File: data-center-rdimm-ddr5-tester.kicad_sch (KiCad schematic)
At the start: 2 parts

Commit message: [#80386] Add company name in board settings
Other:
- company: (none) -> Antmicro
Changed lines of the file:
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@@
 		(date "2023-07-27")
 		(rev "1.0.1")
+		(company "Antmicro")
 		(comment 1 "www.antmicro.com")
-		(comment 2 "Antmicro Ltd")
 	)
 	(text "Data Center RDIMM DDR5 Tester"

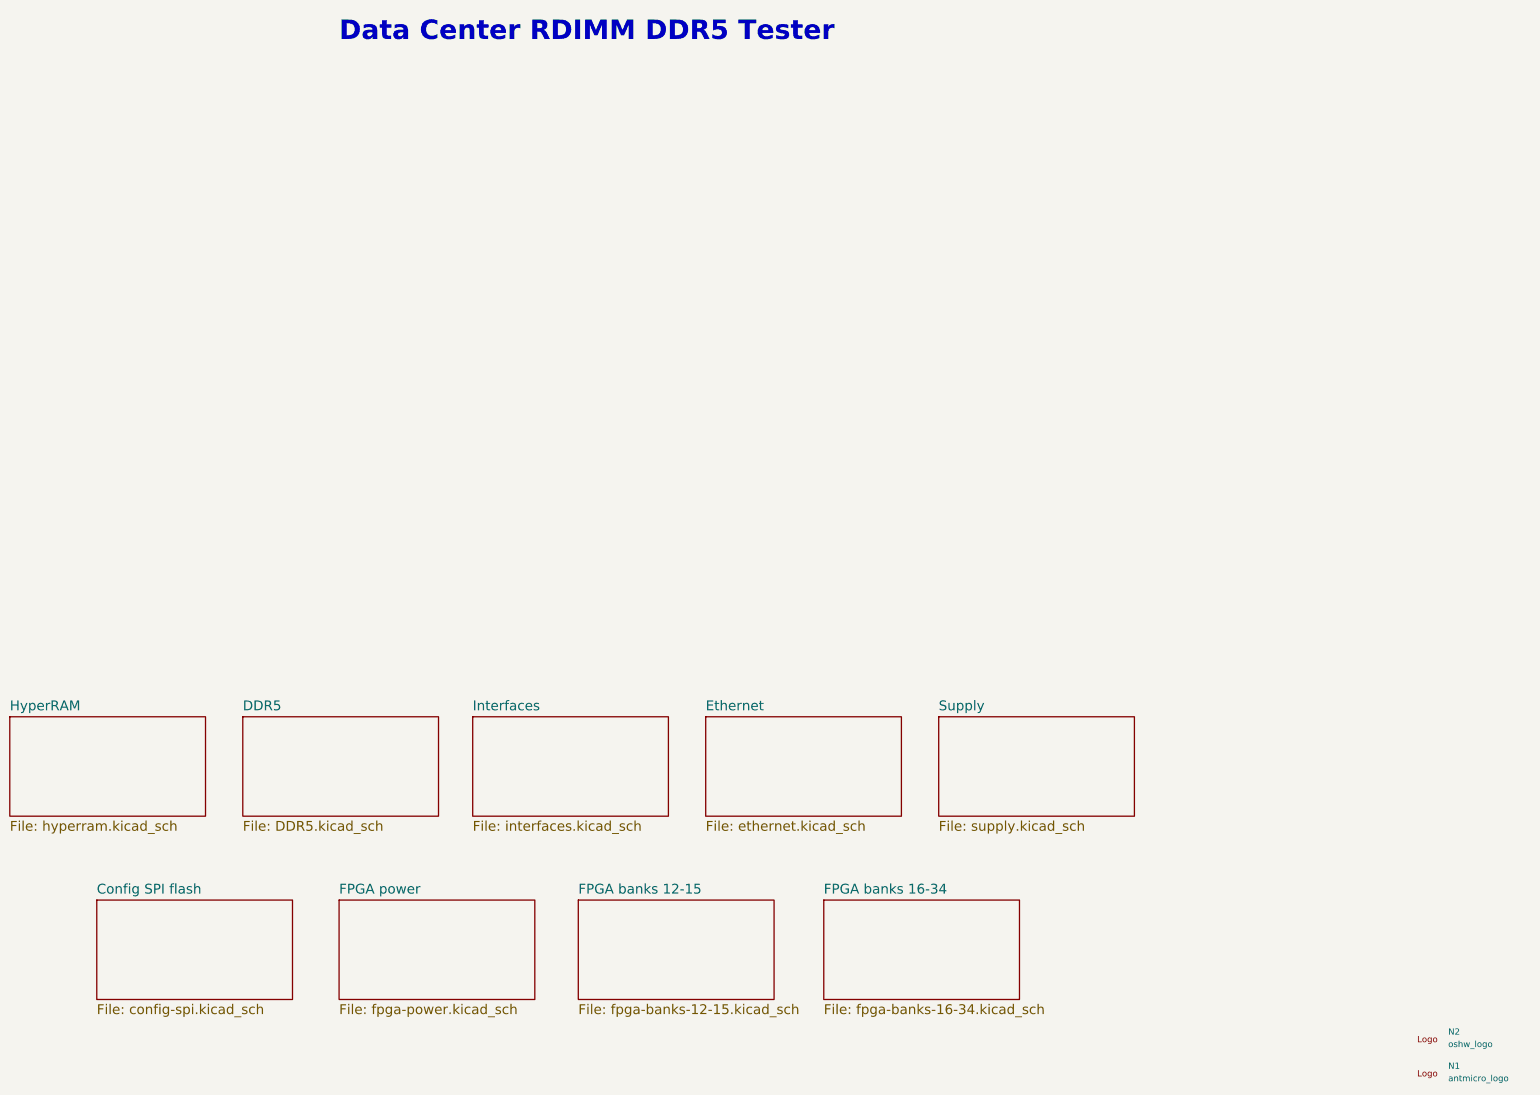
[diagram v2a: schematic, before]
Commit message: [#87036] Update components, clear DRC and ERC
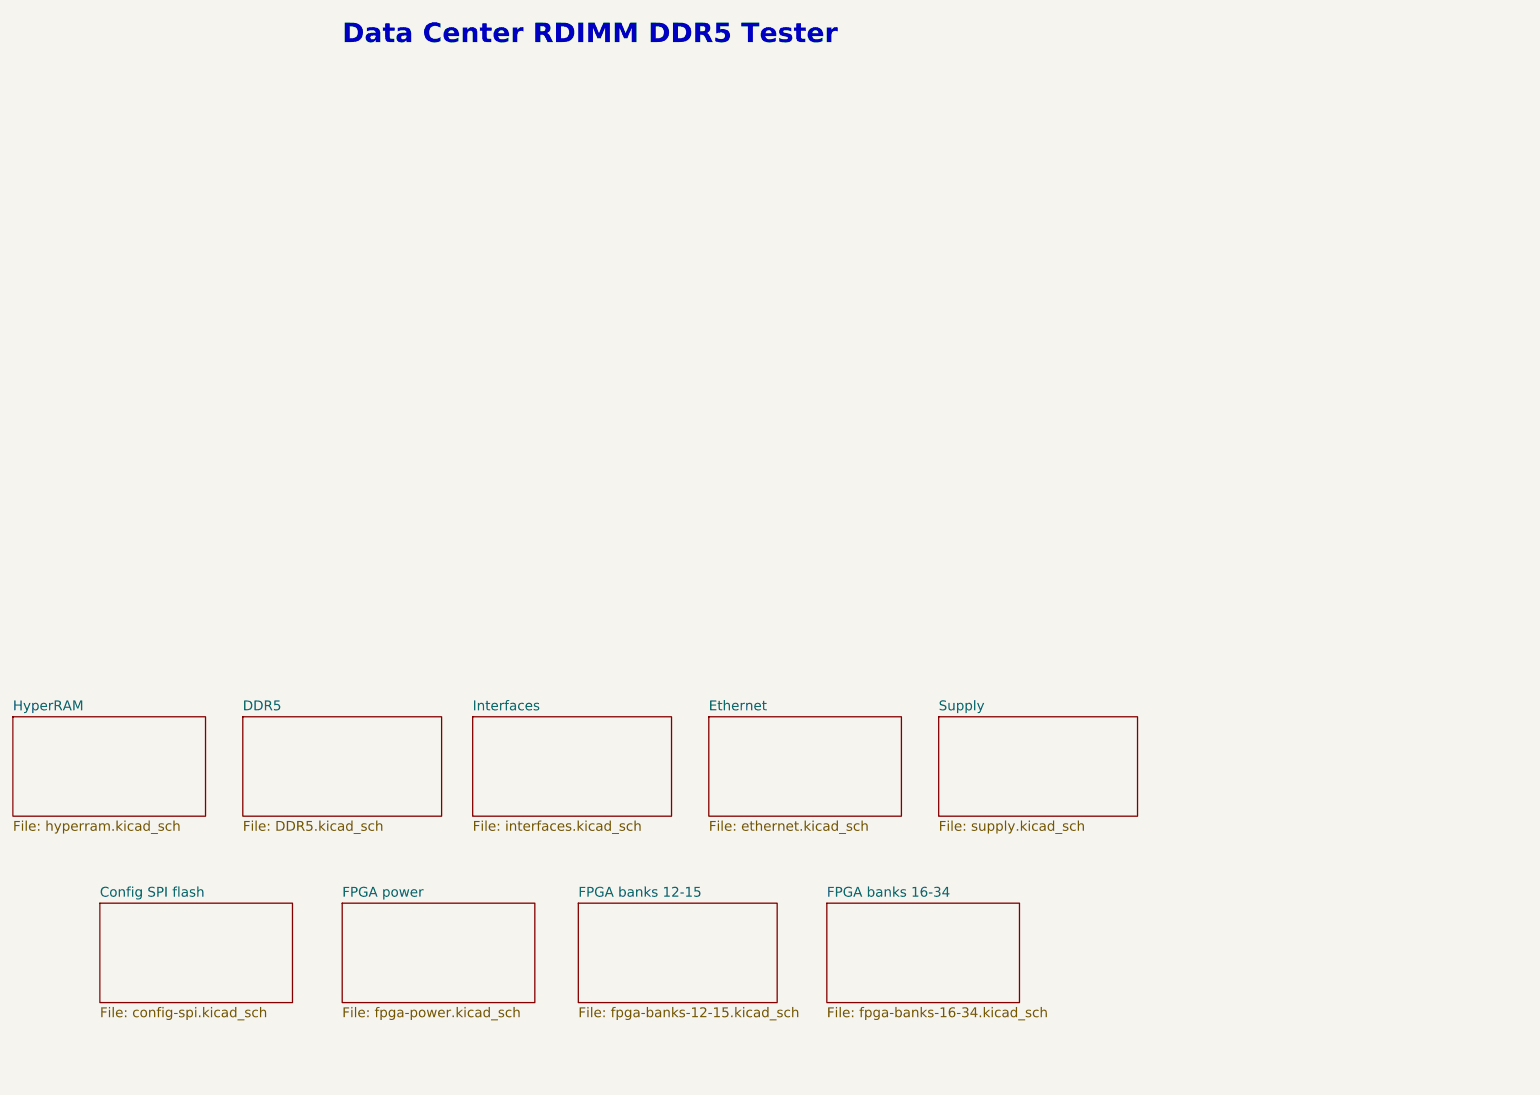
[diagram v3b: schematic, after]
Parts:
- removed N1: antmicro_logo, data-center-rdimm-ddr5-tester-footprints:antmicro-logo_scaled_20mm, symbol data-center-rdimm-ddr5-tester:antmicro_logo
- removed N2: oshw_logo, data-center-rdimm-ddr5-tester-footprints:oshw-logo, symbol data-center-rdimm-ddr5-tester:oshw_logo
